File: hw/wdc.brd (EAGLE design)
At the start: 47.9 x 44.4 mm, 14 parts

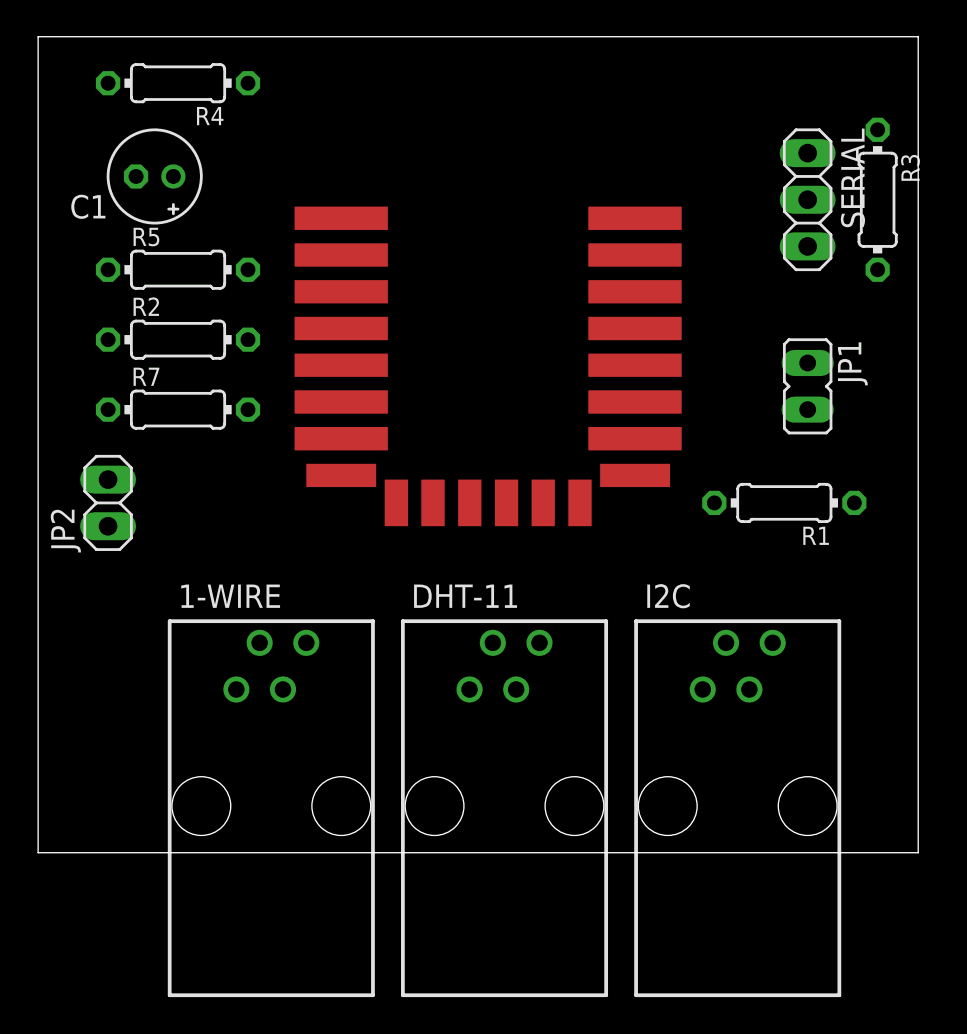
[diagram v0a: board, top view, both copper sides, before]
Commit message: Add natsCmd.js to send commands to the sensors through NATS Add wds.js to subscribe and log messages sent by the sensors through NATS Set temp sensor resolution during startup Change NATS server config to point nano pi neo
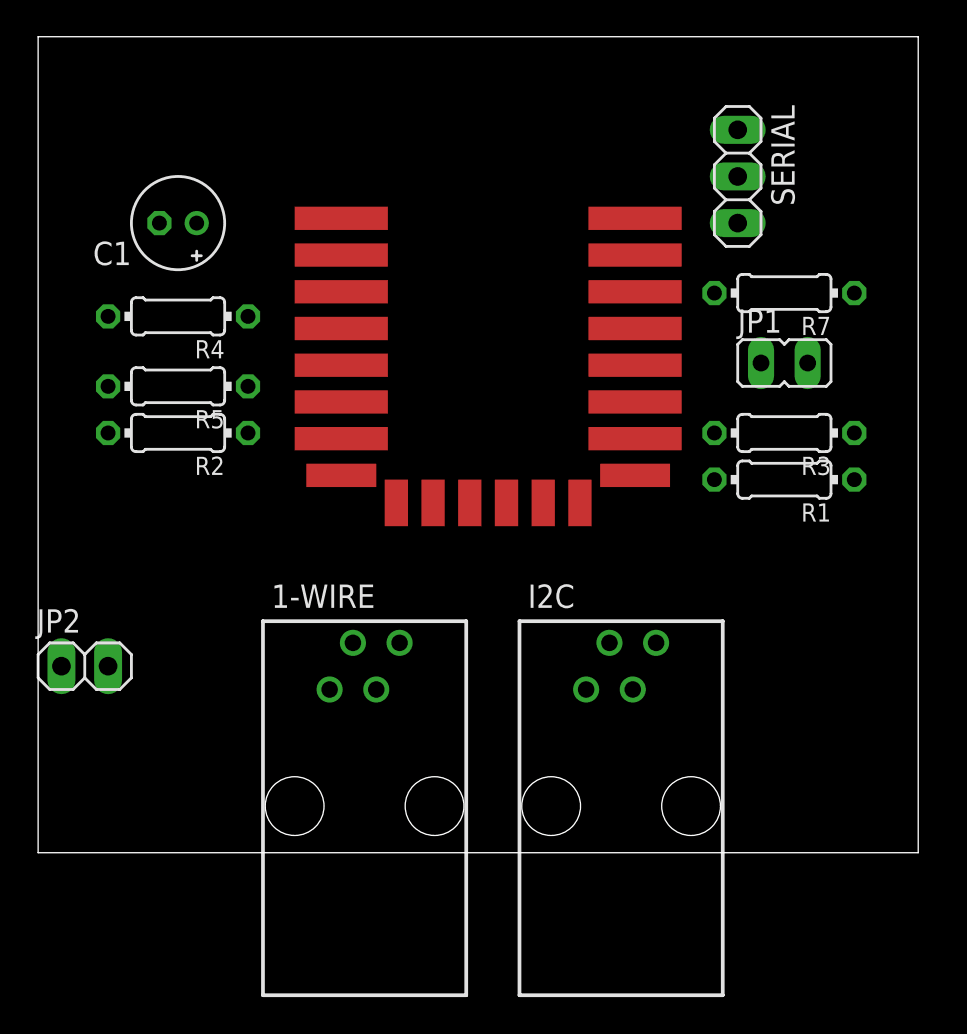
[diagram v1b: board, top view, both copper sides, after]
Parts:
- removed DHT-11: 14867, con-4ucon:14867
- moved R7 33.6 mm to (44.5, 30.5), turned to 180 degrees
- moved R3 13.7 mm to (44.5, 22.9), turned to 180 degrees
- moved R4 12.7 mm to (11.4, 29.2)
- moved JP2 8.98 mm to (6.35, 10.2), turned to 0 degrees
- moved R5 6.35 mm to (11.4, 25.4), turned to 180 degrees
- moved I2C 6.35 mm to (35.6, 2.54)
- moved R2 5.08 mm to (11.4, 22.9), turned to 180 degrees
- moved 1-WIRE 5.08 mm to (21.6, 2.54)
- moved SERIAL 4.02 mm to (41.9, 36.8)
- moved C1 2.84 mm to (11.4, 34.3)
- moved JP1 1.80 mm to (44.5, 26.7), turned to 270 degrees
- moved R1 1.27 mm to (44.5, 20.3)
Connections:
- net 1-WIRE_DATA: no longer 1-WIRE.2
- net DATA: now also 1-WIRE.2; no longer DHT-11.3
- net GND: no longer DHT-11.1
- net VCC: no longer DHT-11.4
